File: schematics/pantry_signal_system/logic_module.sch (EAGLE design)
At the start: 25 parts, among them J10 USBASP_PIN, J5 JST-XH254-3P, J6 JST-XH254-2P, J7 JST-XH254-2P, Q4 STP14NM50N, Q5 2N3904, U10 FAN73611, U11 ATMEGA328P, U12 E220-900T22D, U13 BME280BME280-CONNECTOR-ONLY, U14 2004A I2C

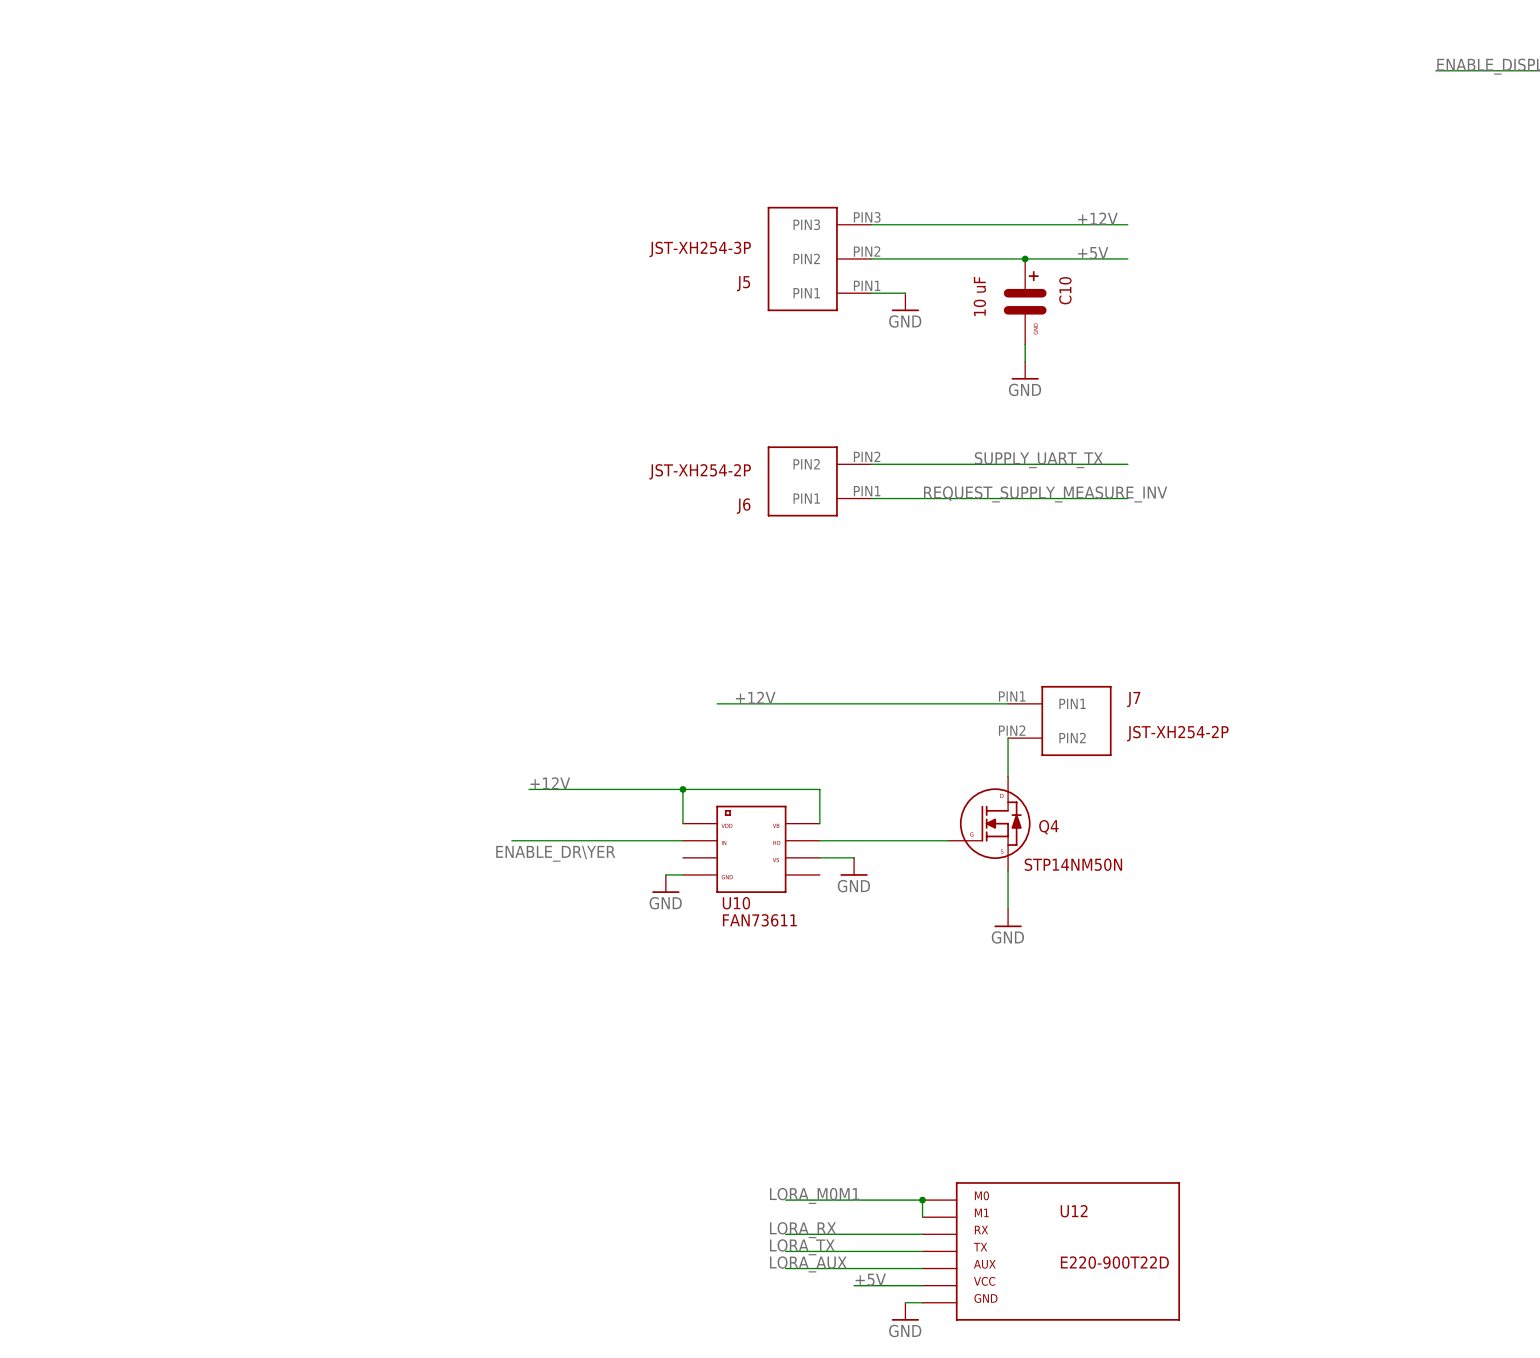
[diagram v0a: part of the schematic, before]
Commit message: Changes in schematics, changes in source code. Current version works too, but I changed boards to fix some possible errors
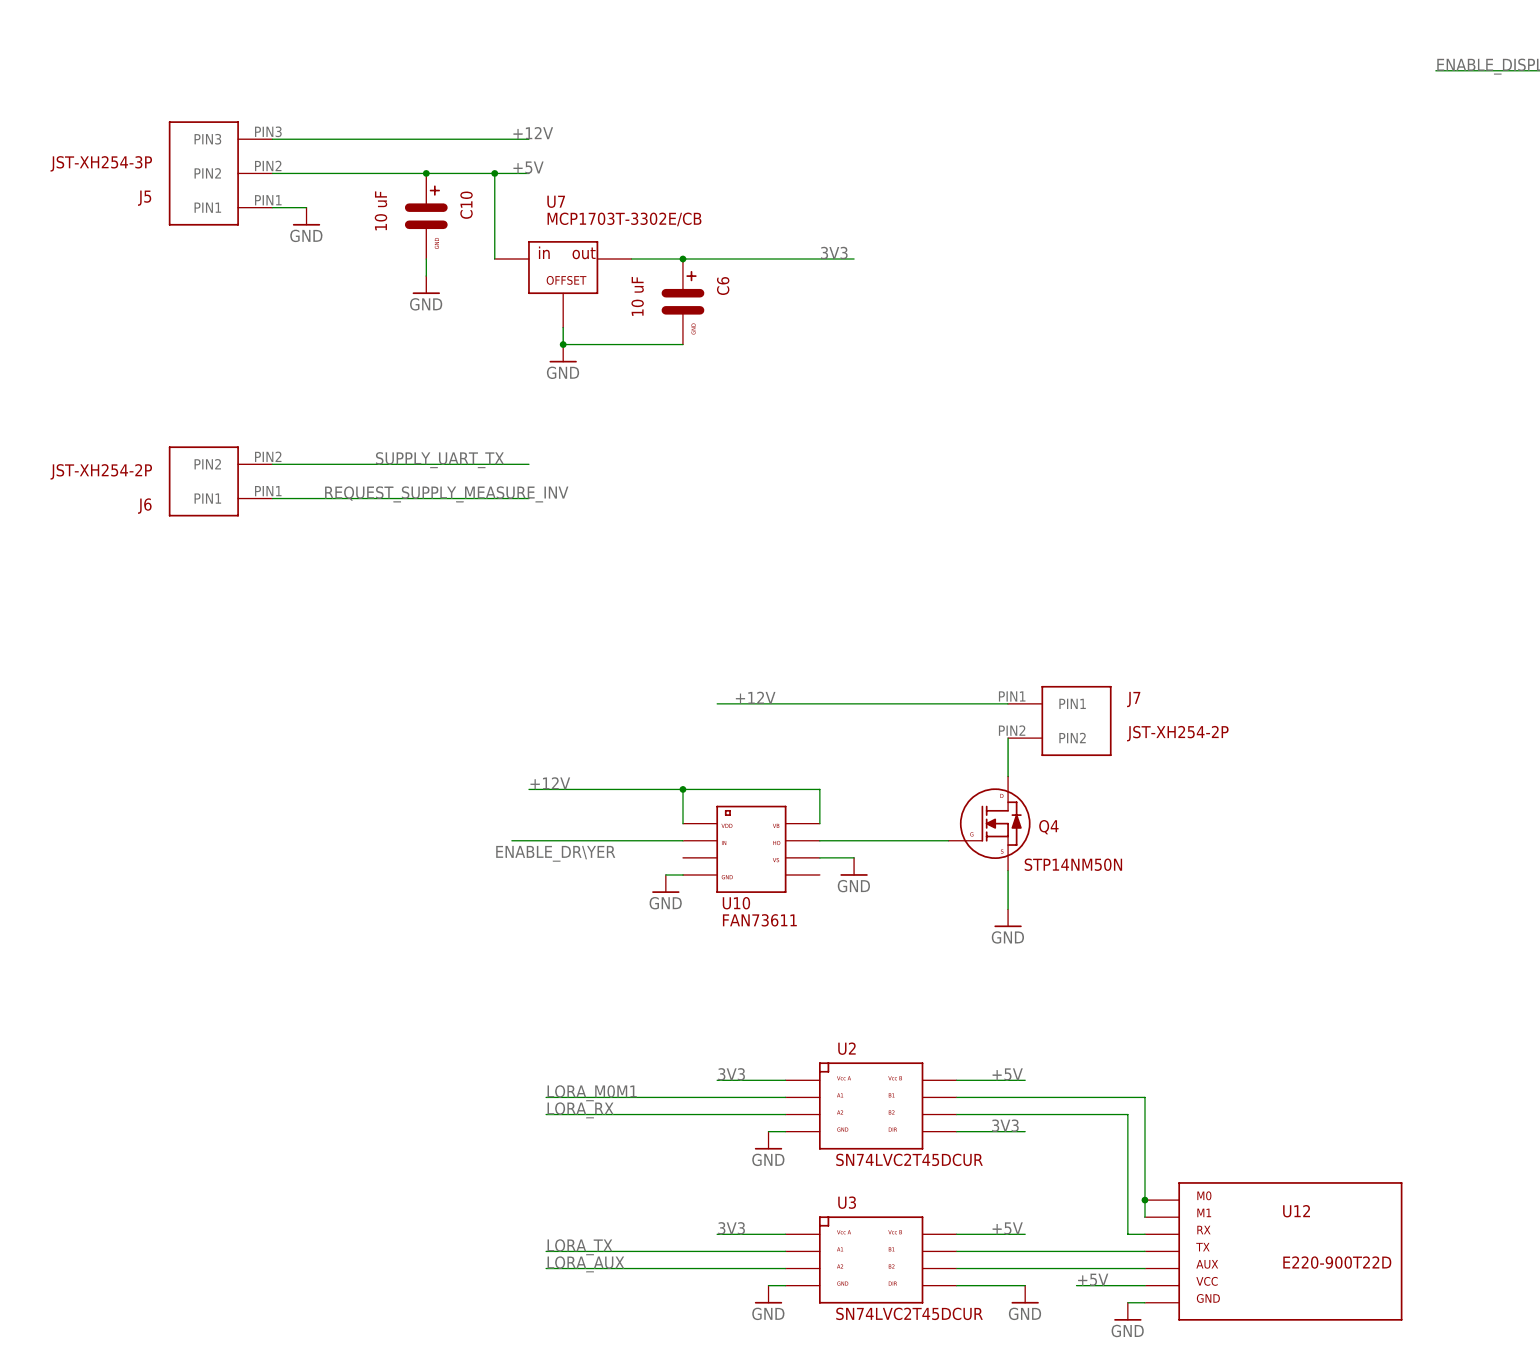
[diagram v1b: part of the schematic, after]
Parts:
- added C6: 10 uF, my_devices:CMINI-5X7
- added U2, U3: SN74LVC2T45DCUR, my_devices:LEVEL_CONVERTER_2L
- added U7: MCP1703T-3302E/CB, my_devices:VOLTAGE_REGULATORSOT-23A
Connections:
- new net 3V3: C6.PIN_PLUS, U2.DIR, U2.VCCA, U3.VCCA, U7.OUT
- new net N$1: U12.TX, U3.B1
- new net N$2: U12.RX, U2.B2
- new net N$3: U12.AUX, U3.B2
- new net N$9: U12.M0, U12.M1, U2.B1
- net +5V: now also U2.VCCB, U3.VCCB, U7.IN
- net GND: now also C6.PIN_GND, U2.GND, U3.DIR, U3.GND, U7.GND
- net LORA_AUX: now also U3.A2; no longer U12.AUX
- net LORA_M0M1: now also U2.A1; no longer U12.M0, U12.M1
- net LORA_RX: now also U2.A2; no longer U12.RX
- net LORA_TX: now also U3.A1; no longer U12.TX
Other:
- moved on the sheet: C10, J5, J6, U12

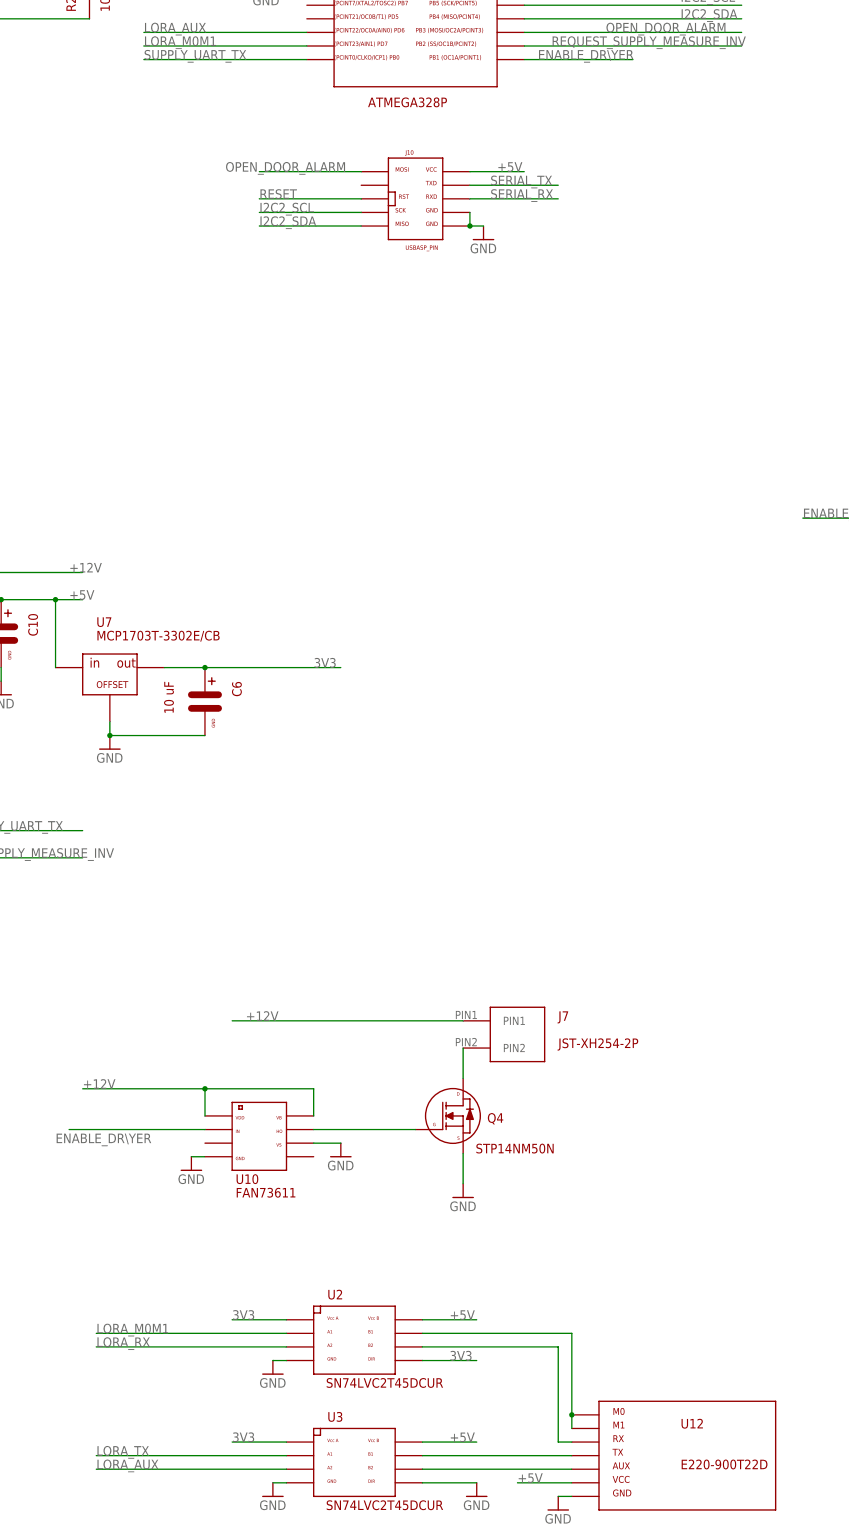
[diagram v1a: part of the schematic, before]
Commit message: Debugging logic module firmware, estabilishing LoRa connection....
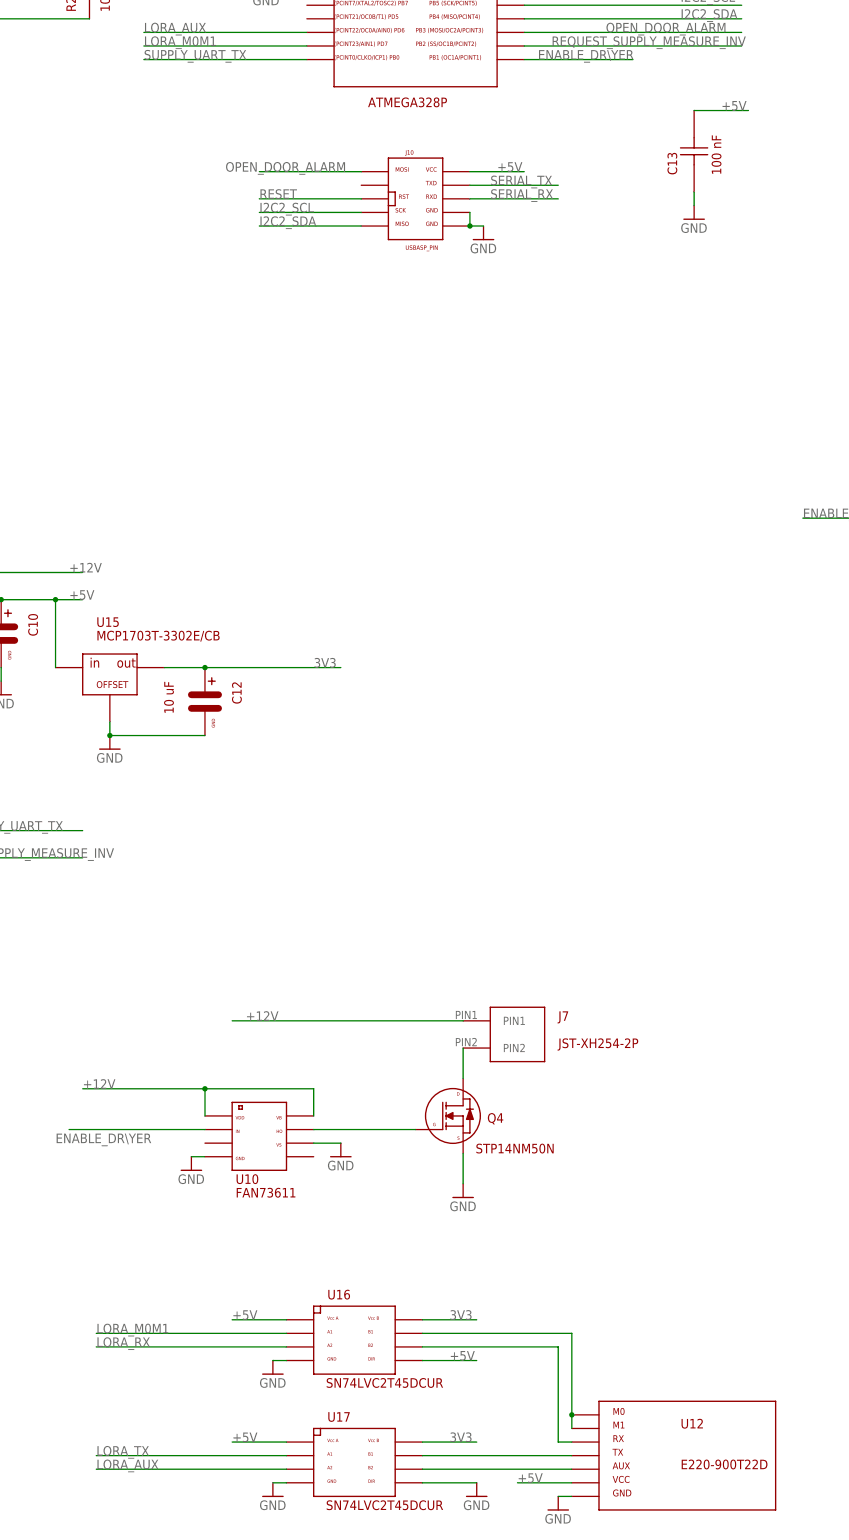
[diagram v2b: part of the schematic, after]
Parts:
- added C13: 100 nF, my_devices:C-1
- renumbered C6 to C12, U2 to U16, U3 to U17, U7 to U15
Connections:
- net +5V: now also C13.P$2, U16.DIR, U16.VCCA, U17.VCCA; no longer U16.VCCB, U17.VCCB
- net 3V3: now also U16.VCCB, U17.VCCB; no longer U16.DIR, U16.VCCA, U17.VCCA
- net GND: now also C13.P$1

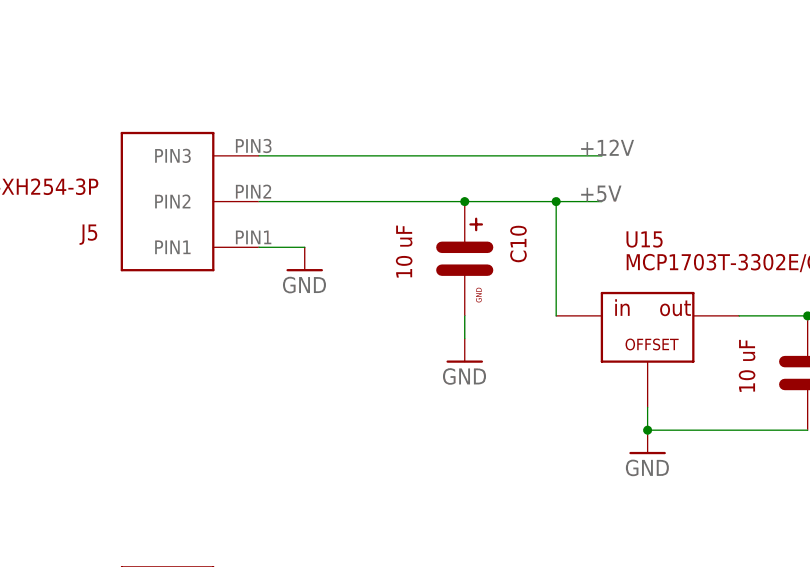
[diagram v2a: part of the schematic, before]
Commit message: Capacitor nominal changed in logic-module to fix problem with chip restart when LoRa sends data with high current consumption
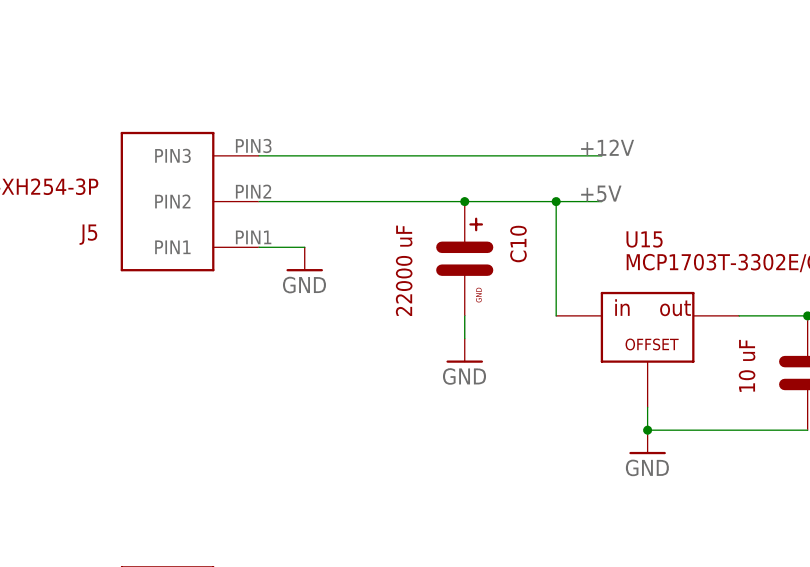
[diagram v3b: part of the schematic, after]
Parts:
- C10: value 10 uF -> 22000 uF
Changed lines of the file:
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@@
 <part name="U14" library="my_devices" deviceset="I2C_DISPLAY" device="" value="2004A I2C"/>
 <part name="Q5" library="my_devices" deviceset="TRANSISTOR_NPN" device="" value="2N3904"/>
-<part name="C10" library="my_devices" deviceset="C" device="MINI-5X7" value="10 uF"/>
+<part name="C10" library="my_devices" deviceset="C" device="MINI-5X7" value="22000 uF"/>
 <part name="GND22" library="supply1" library_urn="urn:adsk.eagle:library:371" deviceset="GND" device=""/>
 <part name="U13" library="my_devices" deviceset="BME280" device="BME280-CONNECTOR-ONLY"/>
